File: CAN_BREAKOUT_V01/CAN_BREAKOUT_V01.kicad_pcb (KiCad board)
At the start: 2 copper layers, 81 x 27.5 mm, 63 parts, among them J1 Conn_01x04, J2 Conn_01x04, J3 Conn_01x04, J4 Conn_01x04, J5 Conn_01x04, J6 Conn_01x04, J7 Conn_01x04, J8 Conn_01x04, Q1 PMOS, U1 LE33CZ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

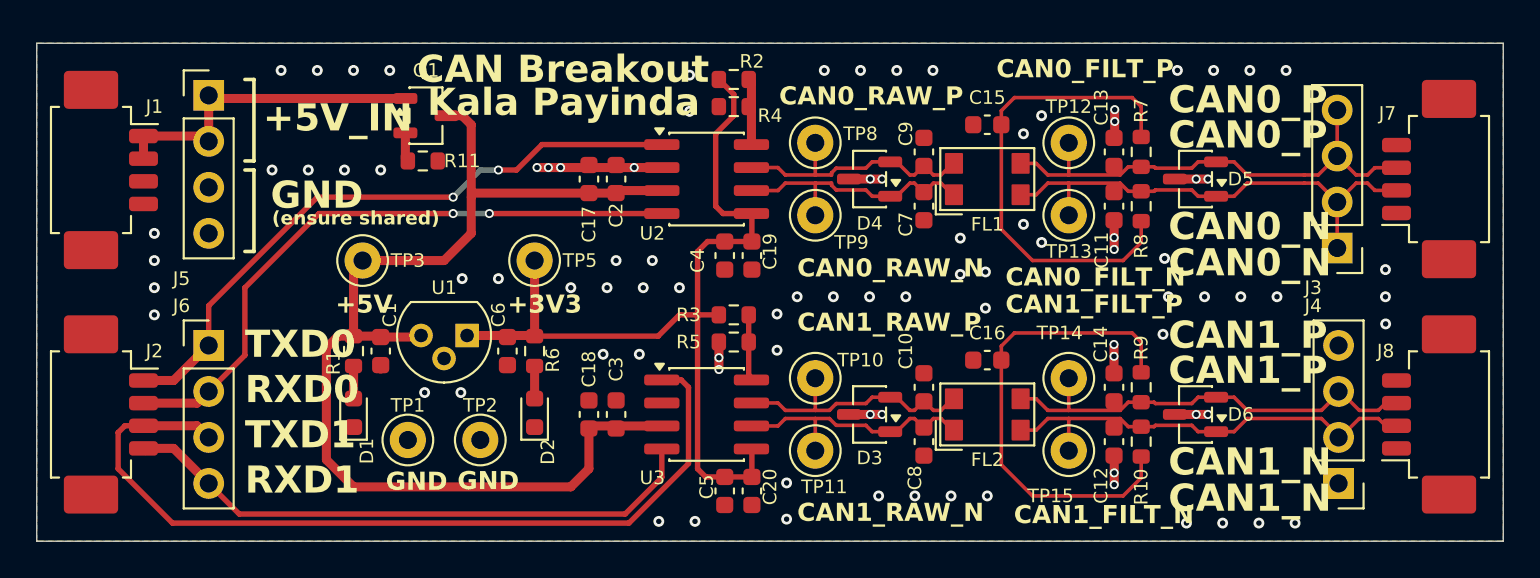
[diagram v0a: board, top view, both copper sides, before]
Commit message: updated to break out SYNC pin to enable MCU control of redundancy channel; still getting text warnings, dont know how to change rules yet..
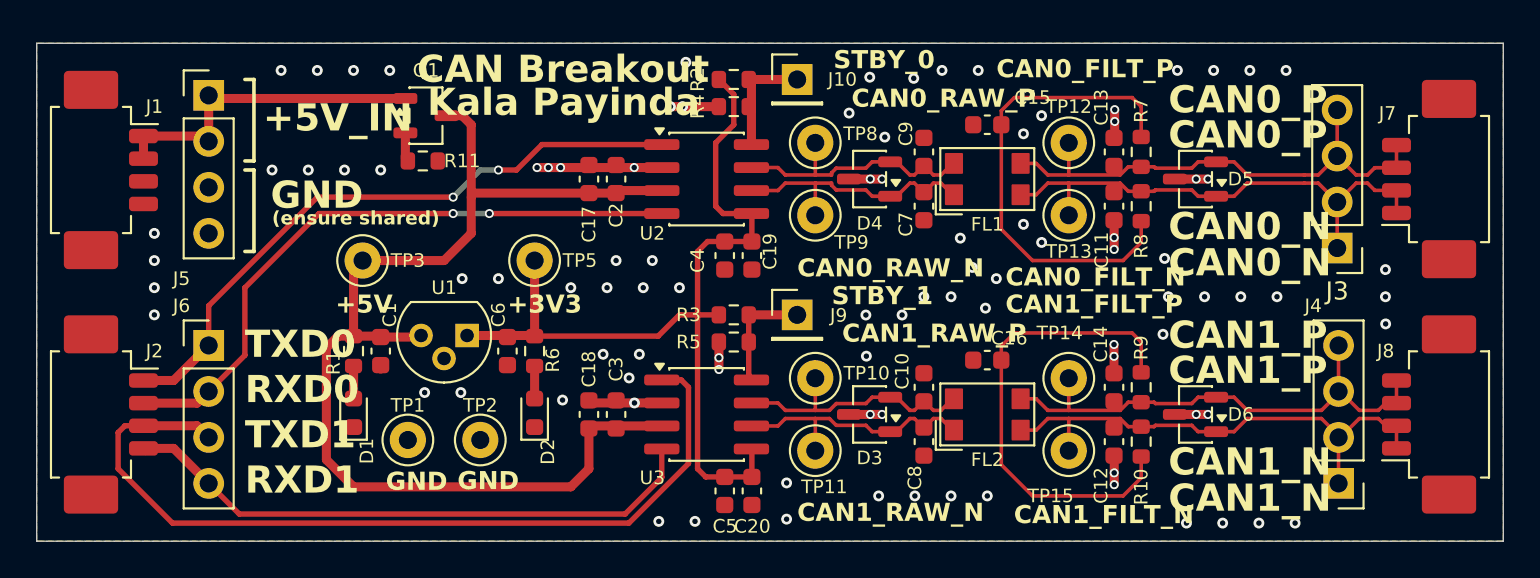
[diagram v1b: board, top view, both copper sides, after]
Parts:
- added J10: Conn_01x01, Connector_PinHeader_2.54mm:PinHeader_1x01_P2.54mm_Vertical, F.Cu at (97.5, 90.5)
- added J9: Conn_01x01, Connector_PinHeader_2.54mm:PinHeader_1x01_P2.54mm_Vertical, F.Cu at (97.5, 103.5)
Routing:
- net GND: track 19.6 -> 26.4 mm, vias 91 -> 96
- net /CAN1_FILT_P: track 25.1 -> 28.9 mm
- net /CAN1_FILT_N: track 25.1 -> 28.9 mm
- net Net-(J9-Pin_1): track 3.68 -> 6.35 mm
- net Net-(J10-Pin_1): track 3.66 -> 6.33 mm
- net /CAN0_FILT_N: track 27.0 -> 28.3 mm
- net /CAN0_FILT_P: track 27.0 -> 28.3 mm
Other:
- board text added: "STBY_0"
- board text added: "STBY_1"

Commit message: ordering this V01 through JLCPCB
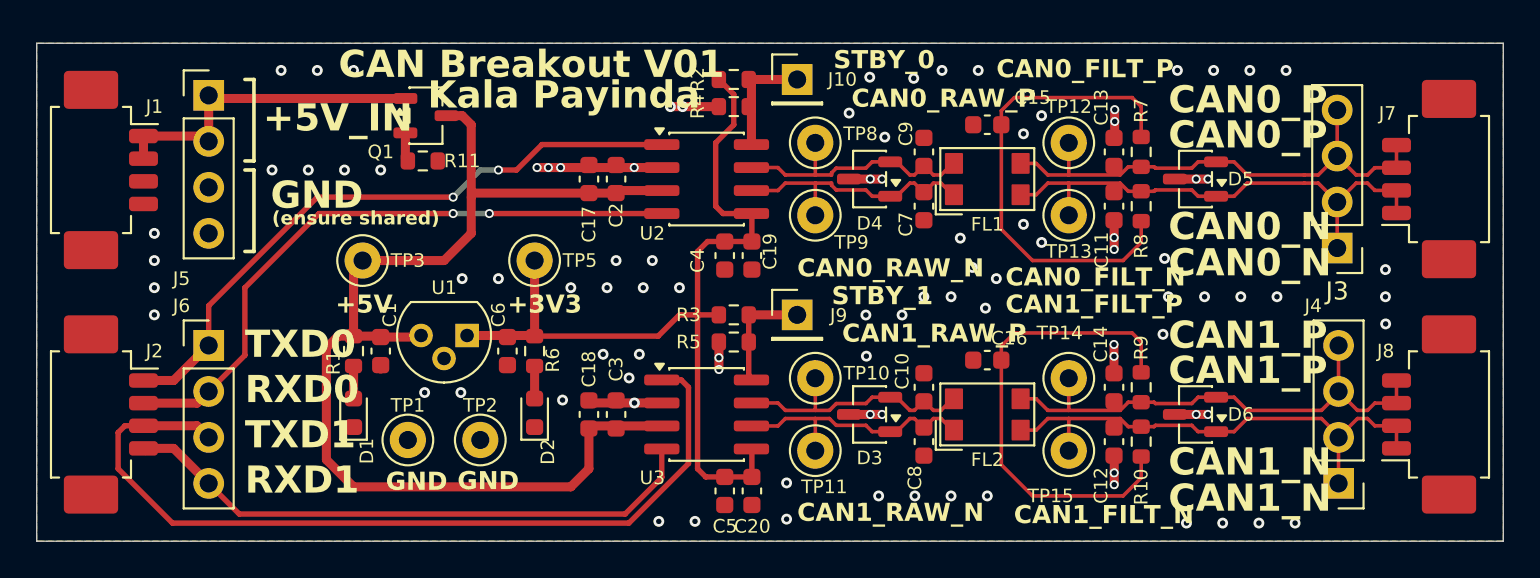
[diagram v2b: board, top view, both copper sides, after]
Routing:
- net /CAN1_FILT_P: track 28.9 -> 29.6 mm
- net /CAN1_FILT_N: track 28.9 -> 29.6 mm
- net GND: vias 96 -> 94
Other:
- board text added: "CAN Breakout V01"
- board text removed: "CAN Breakout"
